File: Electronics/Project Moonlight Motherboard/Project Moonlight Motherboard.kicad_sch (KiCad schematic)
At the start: 44 parts, among them M1 AO3400A, M2 AO3400A, M3 AO3400A, U2 TMC2209_SILENTSTEPSTICK, U3 TMC2209_SILENTSTEPSTICK, U4 TMC2209_SILENTSTEPSTICK, U5 TMC2209_SILENTSTEPSTICK

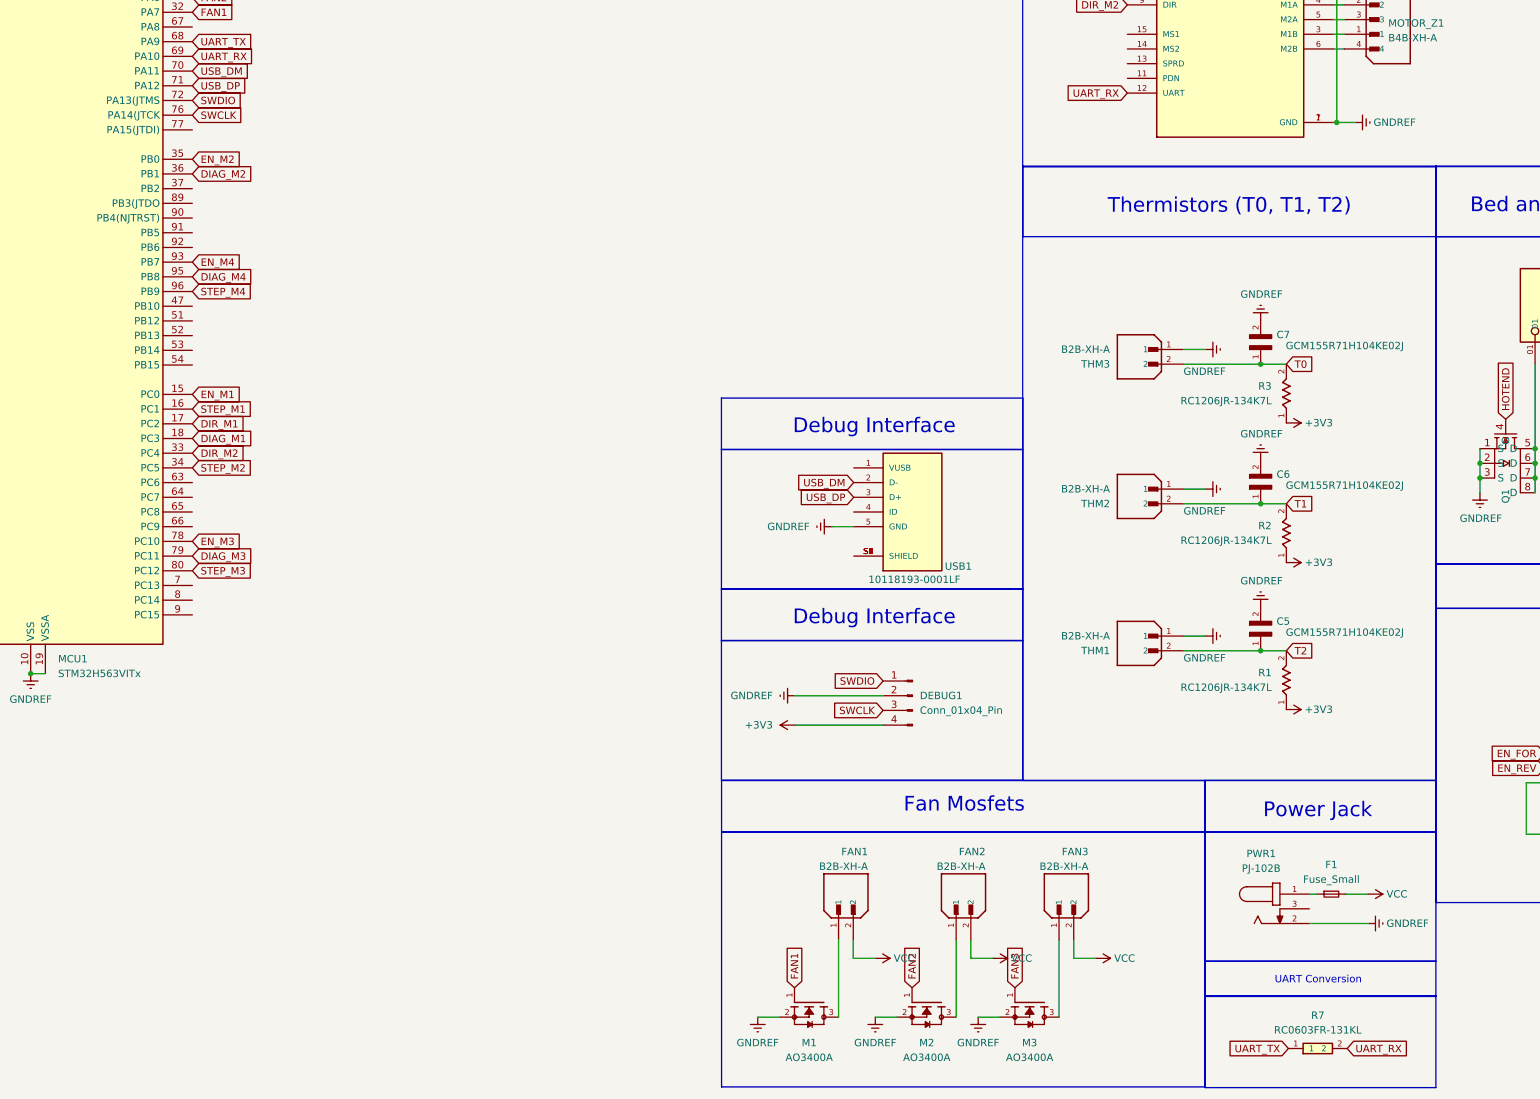
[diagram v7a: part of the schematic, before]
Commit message: added voltage reg, fuse, resistors, etc
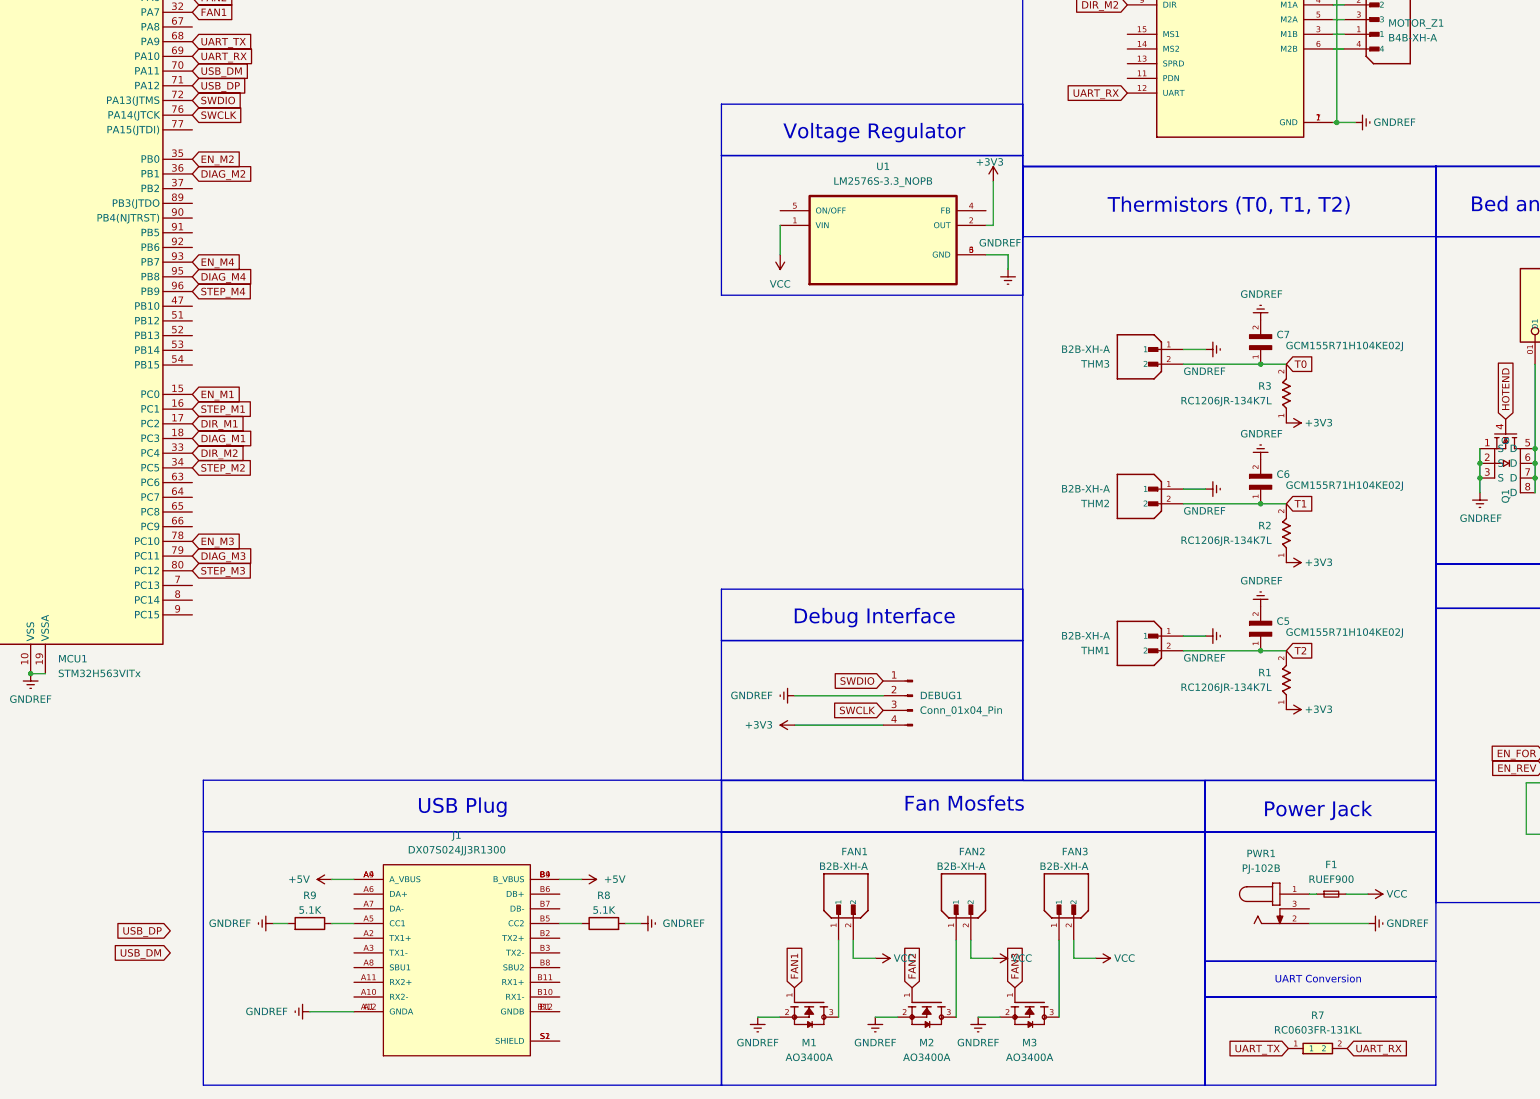
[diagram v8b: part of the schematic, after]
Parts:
- removed USB1: 10118193-0001LF, 10118193-0001LF:AMPHENOL_10118193-0001LF, symbol 10118193-0001LF:10118193-0001LF
- added J1: DX07S024JJ3R1300, DX07S024JJ3R1300:JAE_DX07S024JJ3R1300, symbol DX07S024JJ3R1300:DX07S024JJ3R1300
- added R8, R9: 5.1K, symbol Device:R
- added U1: LM2576S-3.3_NOPB, LM2576S-3.3_NOPB:VREG_TPS79625KTTR, symbol LM2576S-3.3_NOPB:LM2576S-3.3_NOPB
- DEBUG1, REN1, SCRN1: footprint Connector_PinHeader_2.54mm:PinHeader_1x04_P2.54mm_Vertical -> PinHeader:PinHeader_1x04_P2.54mm_Vertical
- F1: value Fuse_Small -> RUEF900; footprint (none) -> RUEF900:FUSRR1015W81L2410T300H2900; now left out of the parts list
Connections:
- net +3V3: now also U1.2 (OUT)
- net GNDREF: now also J1.A1 (GNDA), J1.A12 (GNDA), R8.2, R9.2, U1.3 (GND), U1.6 (GND)
- net VCC: now also U1.1 (VIN)
- new net: J1.A5 (CC1), R9.1
- new net: J1.B5 (CC2), R8.1
- new net: J1.B1 (GNDB), J1.B12 (GNDB)
- new net: J1.S1 (SHIELD), J1.S2 (SHIELD)
- new net +5V: J1.A4 (A_VBUS), J1.A9 (A_VBUS), J1.B4 (B_VBUS), J1.B9 (B_VBUS)
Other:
- note added: "USB Plug"
- note added: "Voltage Regulator"
